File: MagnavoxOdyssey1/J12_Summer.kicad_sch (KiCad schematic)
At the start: 15 parts

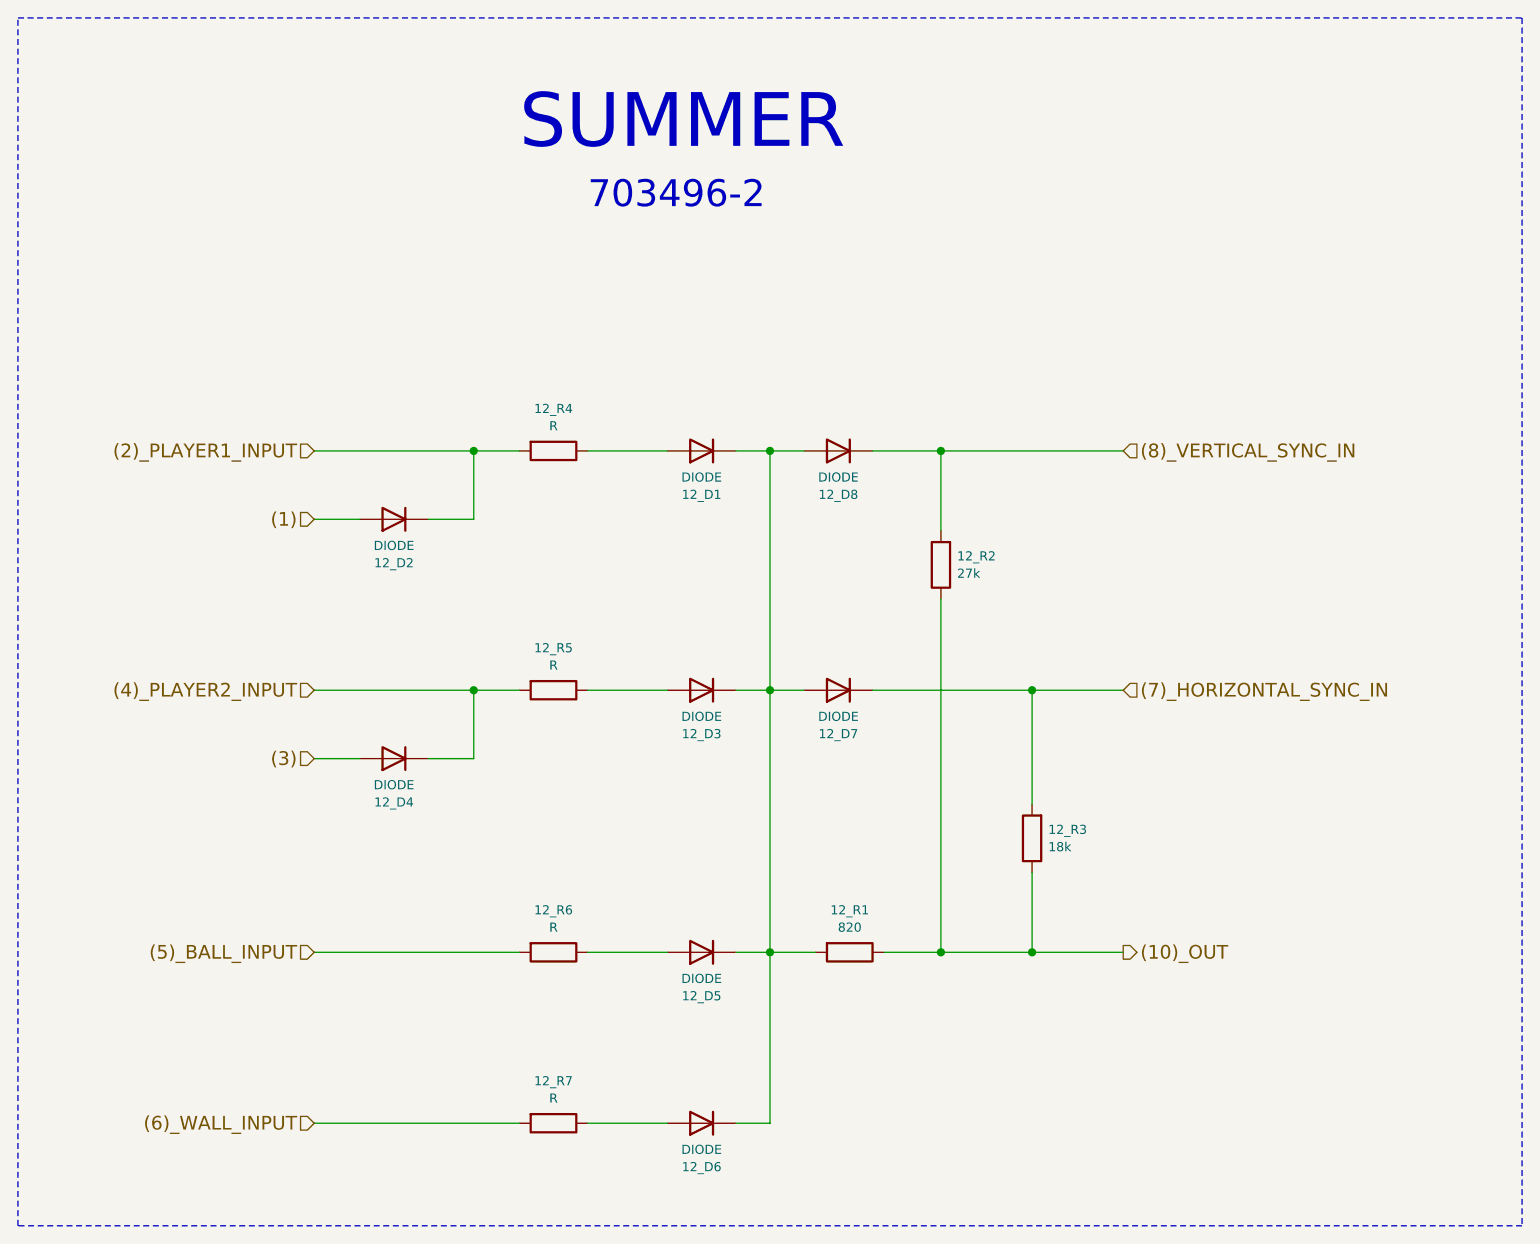
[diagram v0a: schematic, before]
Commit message: update to kicad 9
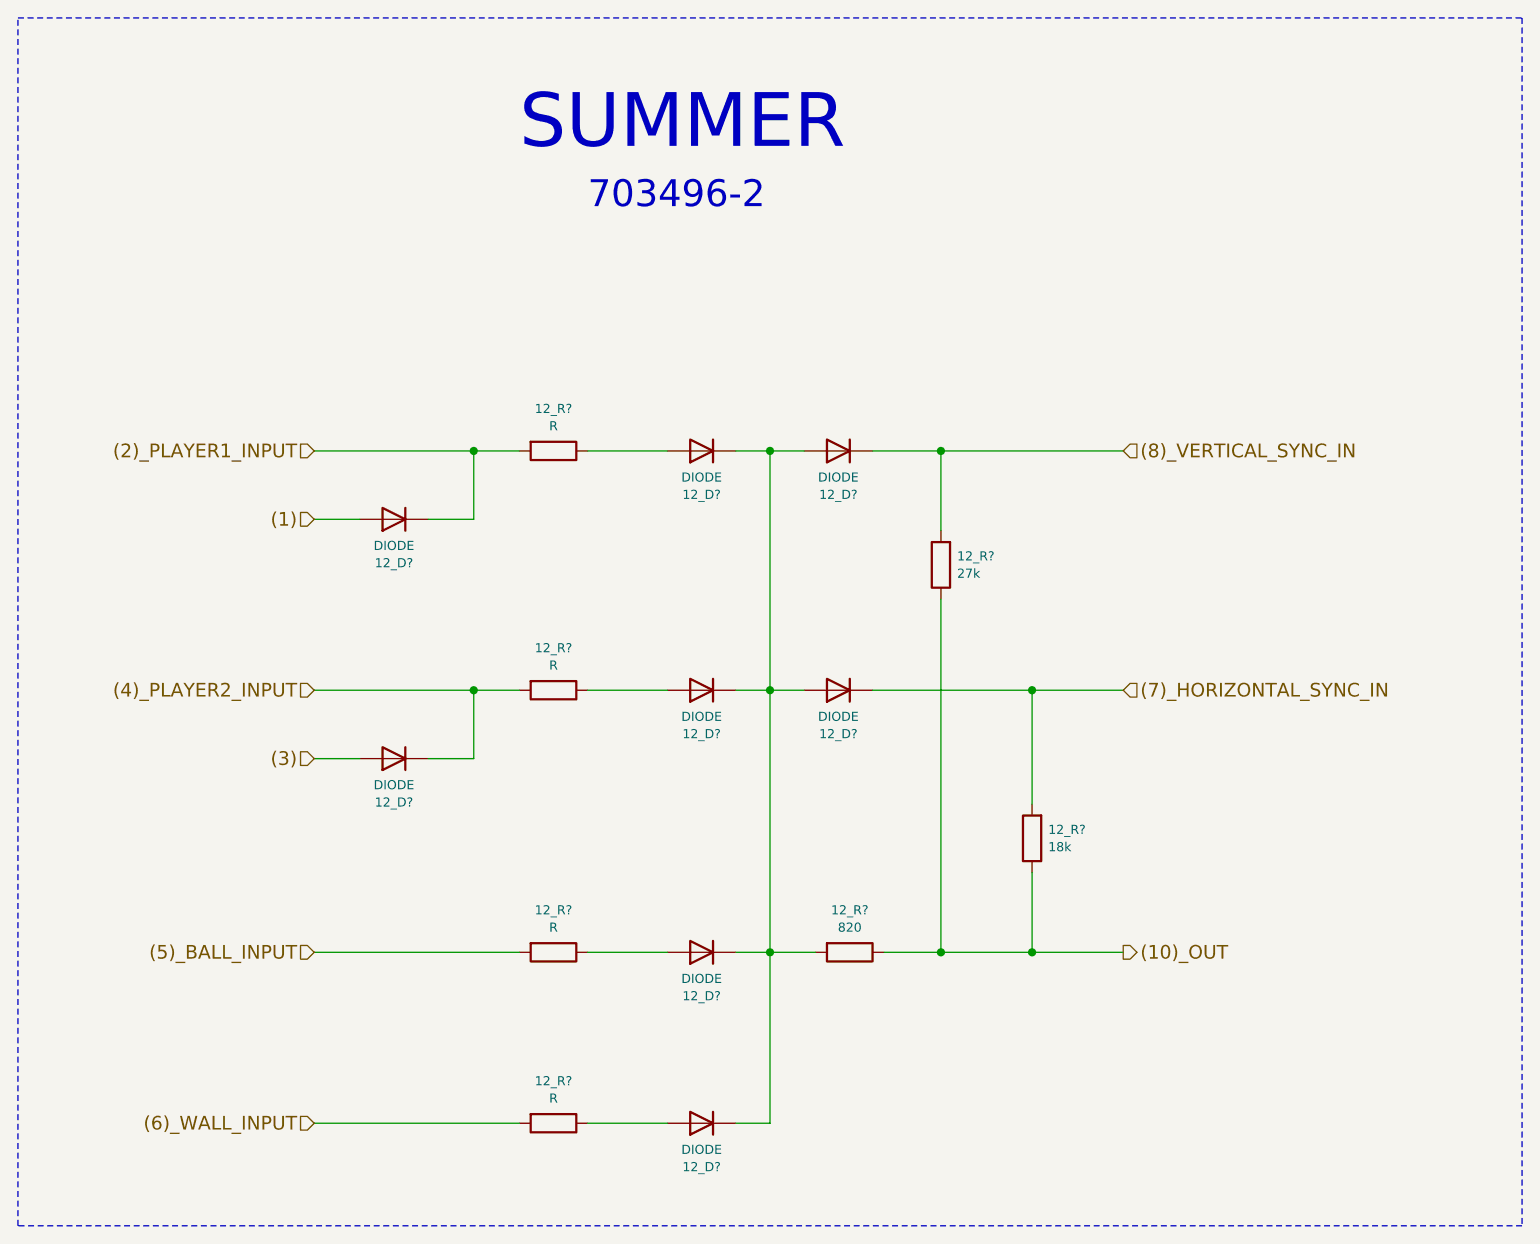
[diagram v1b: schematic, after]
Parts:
- renumbered 12_D1 to 12_D?, 12_D8 to 12_D?, 12_D2 to 12_D?, 12_D3 to 12_D?, 12_D7 to 12_D?, 12_D4 to 12_D?, 12_D5 to 12_D?, 12_D6 to 12_D?, 12_R4 to 12_R?, 12_R5 to 12_R?, 12_R6 to 12_R?, 12_R1 to 12_R?, 12_R7 to 12_R?, 12_R2 to 12_R?, 12_R3 to 12_R?

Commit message: annotate
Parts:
- gave numbers to parts that had none: 15
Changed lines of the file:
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@@
 		(on_board yes)
 		(dnp no)
-		(property "Reference" "12_R?"
+		(property "Reference" "12_R1"
 			(at 124.46 67.691 90)
 			(effects
@@
 			(project "MagnavoxOdyssey1"
 				(path "/adb6e295-eae5-402e-a614-02a705c3e27c/00000000-0000-0000-0000-0000588d6a1d"
-					(reference "12_R?")
+					(reference "12_R1")
 					(unit 1)
 				)
@@
 		(on_board yes)
 		(dnp no)
-		(property "Reference" "12_D?"
+		(property "Reference" "12_D1"
 			(at 140.97 77.2668 0)
 			(effects
@@
 			(project "MagnavoxOdyssey1"
 				(path "/adb6e295-eae5-402e-a614-02a705c3e27c/00000000-0000-0000-0000-0000588d6a1d"
-					(reference "12_D?")
+					(reference "12_D1")
 					(unit 1)
 				)
@@
 		(on_board yes)
 		(dnp no)
-		(property "Reference" "12_D?"
+		(property "Reference" "12_D2"
 			(at 156.21 77.2668 0)
 			(effects
@@
 			(project "MagnavoxOdyssey1"
 				(path "/adb6e295-eae5-402e-a614-02a705c3e27c/00000000-0000-0000-0000-0000588d6a1d"
-					(reference "12_D?")
+					(reference "12_D2")
 					(unit 1)
 				)
@@
 		(on_board yes)
 		(dnp no)
-		(property "Reference" "12_D?"
+		(property "Reference" "12_D3"
 			(at 106.68 84.8868 0)
 			(effects
@@
 			(project "MagnavoxOdyssey1"
 				(path "/adb6e295-eae5-402e-a614-02a705c3e27c/00000000-0000-0000-0000-0000588d6a1d"
-					(reference "12_D?")
+					(reference "12_D3")
 					(unit 1)
 				)
@@
 		(on_board yes)
 		(dnp no)
-		(property "Reference" "12_R?"
+		(property "Reference" "12_R3"
 			(at 124.46 94.361 90)
 			(effects
@@
 			(project "MagnavoxOdyssey1"
 				(path "/adb6e295-eae5-402e-a614-02a705c3e27c/00000000-0000-0000-0000-0000588d6a1d"
-					(reference "12_R?")
+					(reference "12_R3")
 					(unit 1)
 				)
@@
 		(on_board yes)
 		(dnp no)
-		(property "Reference" "12_D?"
+		(property "Reference" "12_D4"
 			(at 140.97 103.9368 0)
 			(effects
@@
 			(project "MagnavoxOdyssey1"
 				(path "/adb6e295-eae5-402e-a614-02a705c3e27c/00000000-0000-0000-0000-0000588d6a1d"
-					(reference "12_D?")
+					(reference "12_D4")
 					(unit 1)
 				)
@@
 		(on_board yes)
 		(dnp no)
-		(property "Reference" "12_D?"
+		(property "Reference" "12_D5"
 			(at 156.21 103.9368 0)
 			(effects
@@
 			(project "MagnavoxOdyssey1"
 				(path "/adb6e295-eae5-402e-a614-02a705c3e27c/00000000-0000-0000-0000-0000588d6a1d"
-					(reference "12_D?")
+					(reference "12_D5")
 					(unit 1)
 				)
@@
 		(on_board yes)
 		(dnp no)
-		(property "Reference" "12_D?"
+		(property "Reference" "12_D6"
 			(at 106.68 111.5568 0)
 			(effects
@@
 			(project "MagnavoxOdyssey1"
 				(path "/adb6e295-eae5-402e-a614-02a705c3e27c/00000000-0000-0000-0000-0000588d6a1d"
-					(reference "12_D?")
+					(reference "12_D6")
 					(unit 1)
 				)
@@
 		(on_board yes)
 		(dnp no)
-		(property "Reference" "12_R?"
+		(property "Reference" "12_R5"
 			(at 124.46 123.571 90)
 			(effects
@@
 			(project "MagnavoxOdyssey1"
 				(path "/adb6e295-eae5-402e-a614-02a705c3e27c/00000000-0000-0000-0000-0000588d6a1d"
-					(reference "12_R?")
+					(reference "12_R5")
 					(unit 1)
 				)
@@
 		(on_board yes)
 		(dnp no)
-		(property "Reference" "12_D?"
+		(property "Reference" "12_D7"
 			(at 140.97 133.1468 0)
 			(effects
@@
 			(project "MagnavoxOdyssey1"
 				(path "/adb6e295-eae5-402e-a614-02a705c3e27c/00000000-0000-0000-0000-0000588d6a1d"
-					(reference "12_D?")
+					(reference "12_D7")
 					(unit 1)
 				)
@@
 		(on_board yes)
 		(dnp no)
-		(property "Reference" "12_R?"
+		(property "Reference" "12_R6"
 			(at 157.48 123.571 90)
 			(effects
@@
 			(project "MagnavoxOdyssey1"
 				(path "/adb6e295-eae5-402e-a614-02a705c3e27c/00000000-0000-0000-0000-0000588d6a1d"
-					(reference "12_R?")
+					(reference "12_R6")
 					(unit 1)
 				)
@@
 		(on_board yes)
 		(dnp no)
-		(property "Reference" "12_R?"
+		(property "Reference" "12_R7"
 			(at 124.46 142.621 90)
 			(effects
@@
 			(project "MagnavoxOdyssey1"
 				(path "/adb6e295-eae5-402e-a614-02a705c3e27c/00000000-0000-0000-0000-0000588d6a1d"
-					(reference "12_R?")
+					(reference "12_R7")
 					(unit 1)
 				)
@@
 		(on_board yes)
 		(dnp no)
-		(property "Reference" "12_D?"
+		(property "Reference" "12_D8"
 			(at 140.97 152.1968 0)
 			(effects
@@
 			(project "MagnavoxOdyssey1"
 				(path "/adb6e295-eae5-402e-a614-02a705c3e27c/00000000-0000-0000-0000-0000588d6a1d"
-					(reference "12_D?")
+					(reference "12_D8")
 					(unit 1)
 				)
@@
 		(on_board yes)
 		(dnp no)
-		(property "Reference" "12_R?"
+		(property "Reference" "12_R2"
 			(at 169.4434 84.1248 0)
 			(effects
@@
 			(project "MagnavoxOdyssey1"
 				(path "/adb6e295-eae5-402e-a614-02a705c3e27c/00000000-0000-0000-0000-0000588d6a1d"
-					(reference "12_R?")
+					(reference "12_R2")
 					(unit 1)
 				)
@@
 		(on_board yes)
 		(dnp no)
-		(property "Reference" "12_R?"
+		(property "Reference" "12_R4"
 			(at 179.6034 114.6048 0)
 			(effects
@@
 			(project "MagnavoxOdyssey1"
 				(path "/adb6e295-eae5-402e-a614-02a705c3e27c/00000000-0000-0000-0000-0000588d6a1d"
-					(reference "12_R?")
-					(unit 1)
-				)
+					(reference "12_R4")
+					(unit 1)
+				)
